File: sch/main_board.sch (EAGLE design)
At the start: 19 parts, among them IC1 MCP73831T-2ACI_OT, J1 MICRO_USB_B_HIROSE_ZX62-B-5PA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

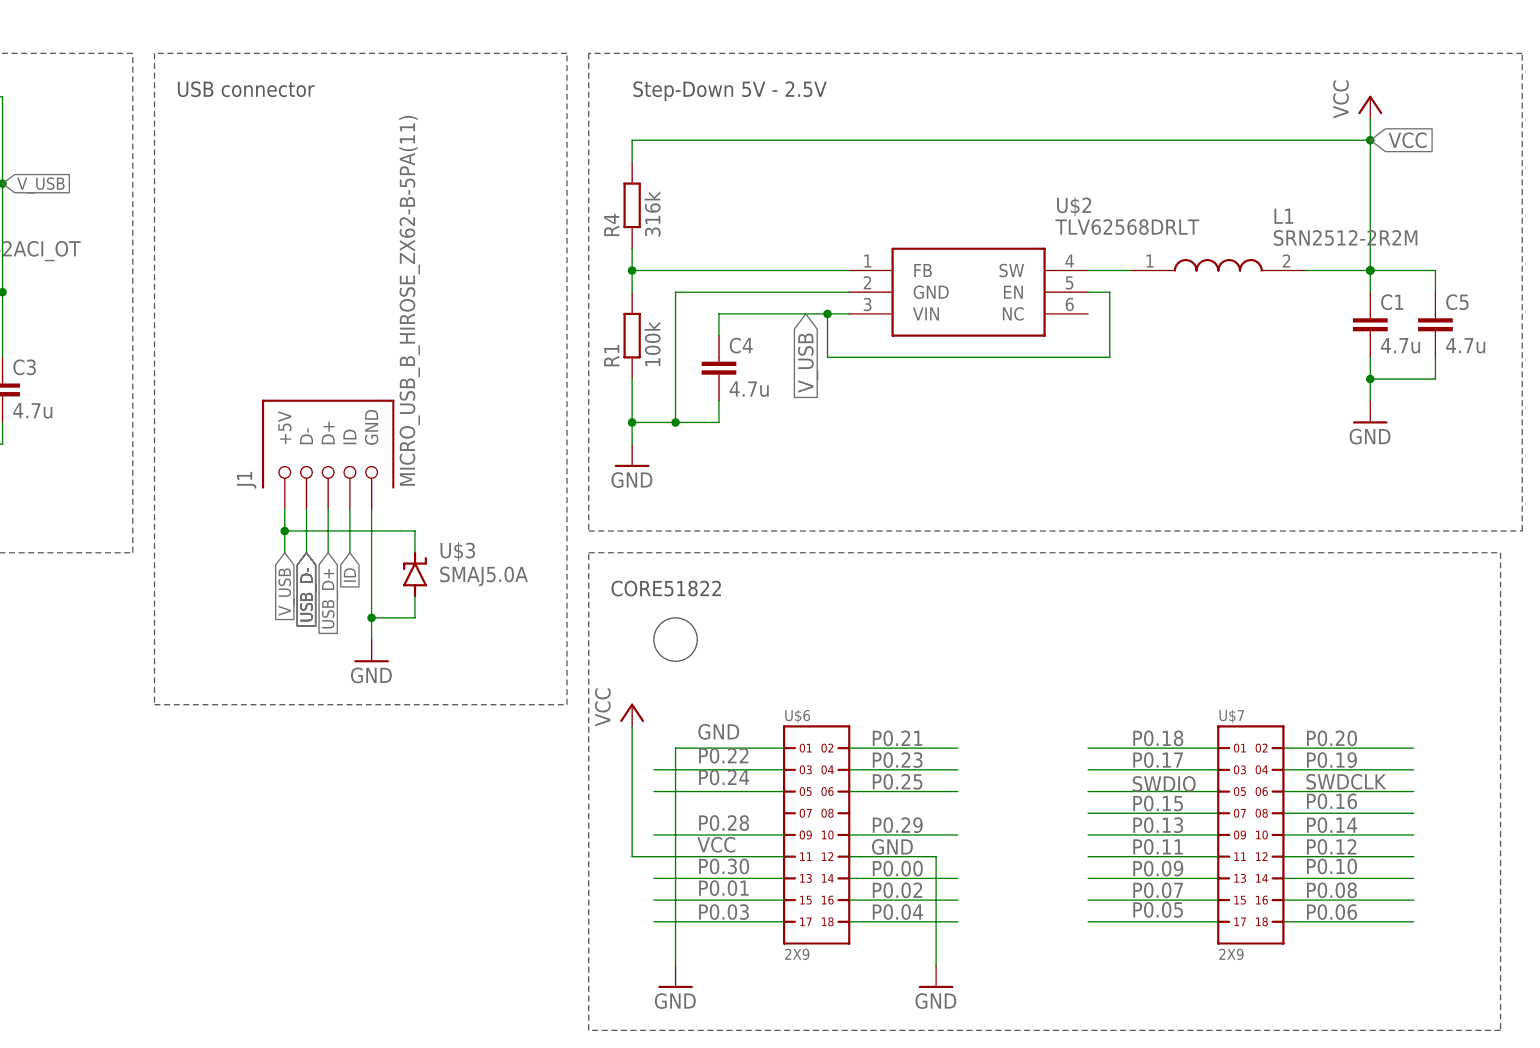
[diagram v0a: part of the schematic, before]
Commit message: Add docs for STM32WB, Remove unused power supply elements.
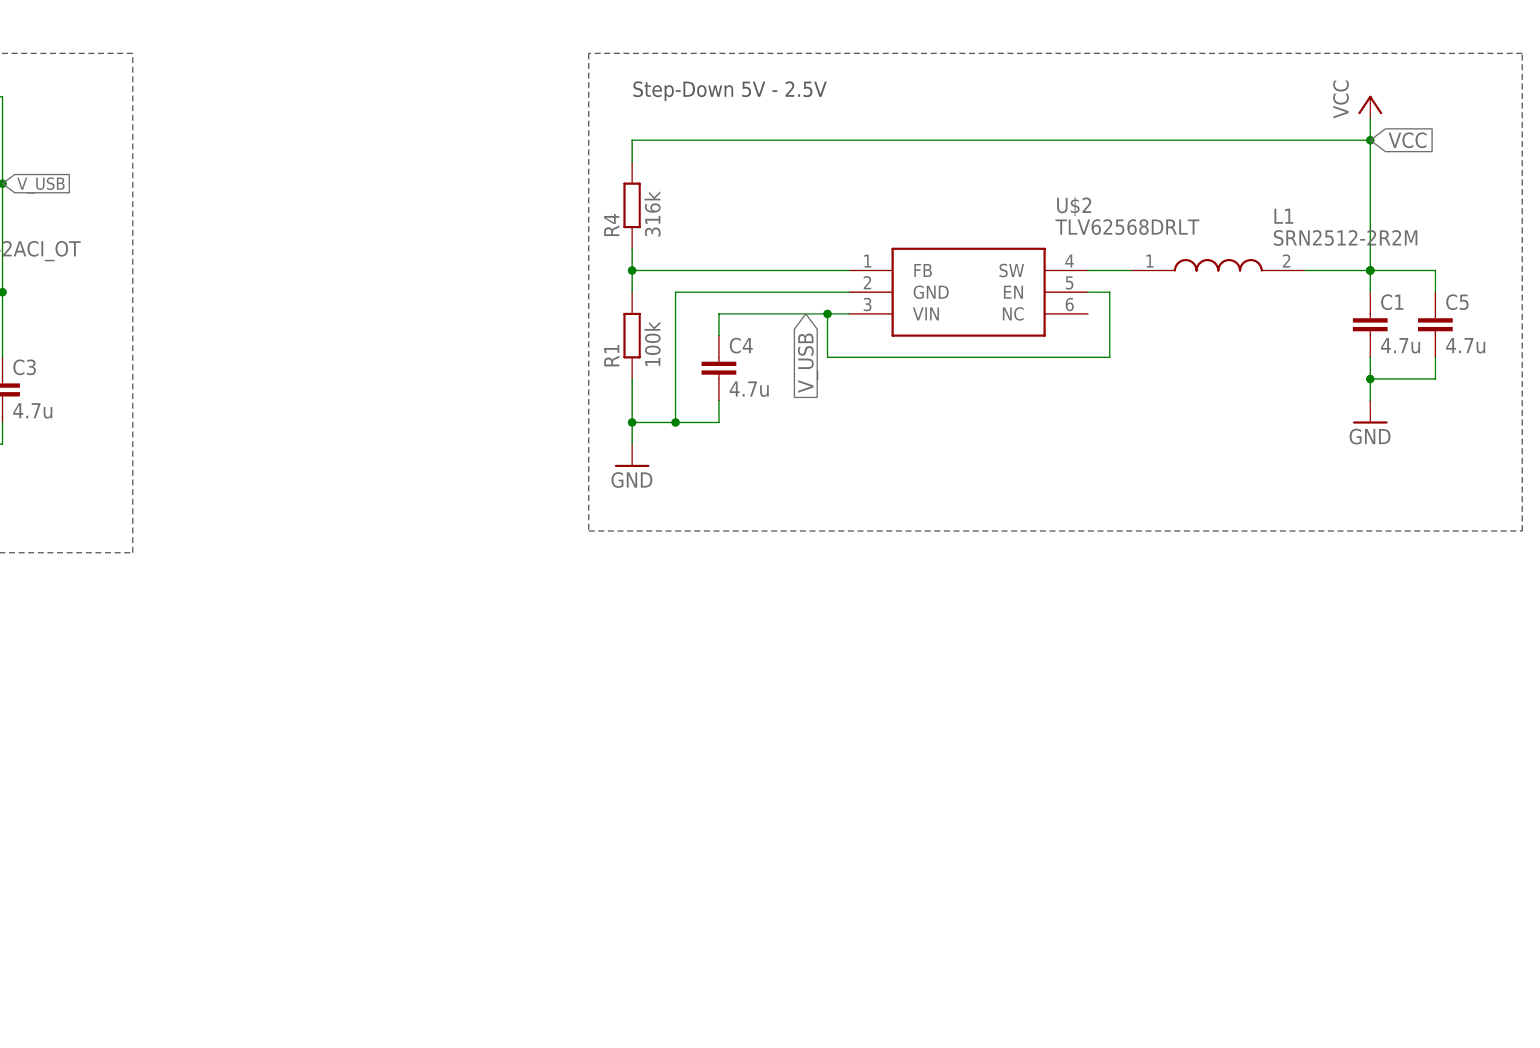
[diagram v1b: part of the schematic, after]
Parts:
- removed J1: MICRO_USB_B_HIROSE_ZX62-B-5PA(11), connector:MICRO_USB_B_HIROSE_ZX62-B-5PA(11)
- removed U$3: SMAJ5.0A, SamacSys_Parts:SMAJ5.0A
- removed U$6, U$7: 2X9, headers(2mm):2X9
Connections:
- removed net ID: J1.ID
- removed net P0.00: U$6.14
- removed net P0.01: U$6.15
- removed net P0.02: U$6.16
- removed net P0.03: U$6.17
- removed net P0.04: U$6.18
- removed net P0.05: U$7.17
- removed net P0.06: U$7.18
- removed net P0.07: U$7.15
- removed net P0.08: U$7.16
- removed net P0.09: U$7.13
- removed net P0.10: U$7.14
- removed net P0.11: U$7.11
- removed net P0.12: U$7.12
- removed net P0.13: U$7.9
- removed net P0.14: U$7.10
- removed net P0.15: U$7.7
- removed net P0.16: U$7.8
- removed net P0.17: U$7.3
- removed net P0.18: U$7.1
- removed net P0.19: U$7.4
- removed net P0.20: U$7.2
- removed net P0.21: U$6.2
- removed net P0.22: U$6.3
- removed net P0.23: U$6.4
- removed net P0.24: U$6.5
- removed net P0.25: U$6.6
- removed net P0.28: U$6.9
- removed net P0.29: U$6.10
- removed net P0.30: U$6.13
- removed net SWDCLK: U$7.6
- removed net SWDIO: U$7.5
- removed net USB_D+: J1.D+
- removed net USB_D-: J1.D-
- net GND: no longer J1.GND, U$3.A, U$6.1, U$6.12
- net VCC: no longer U$6.11
- net V_USB: no longer J1.+5V, U$3.C
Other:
- note removed: "CORE51822"
- note removed: "USB connector"

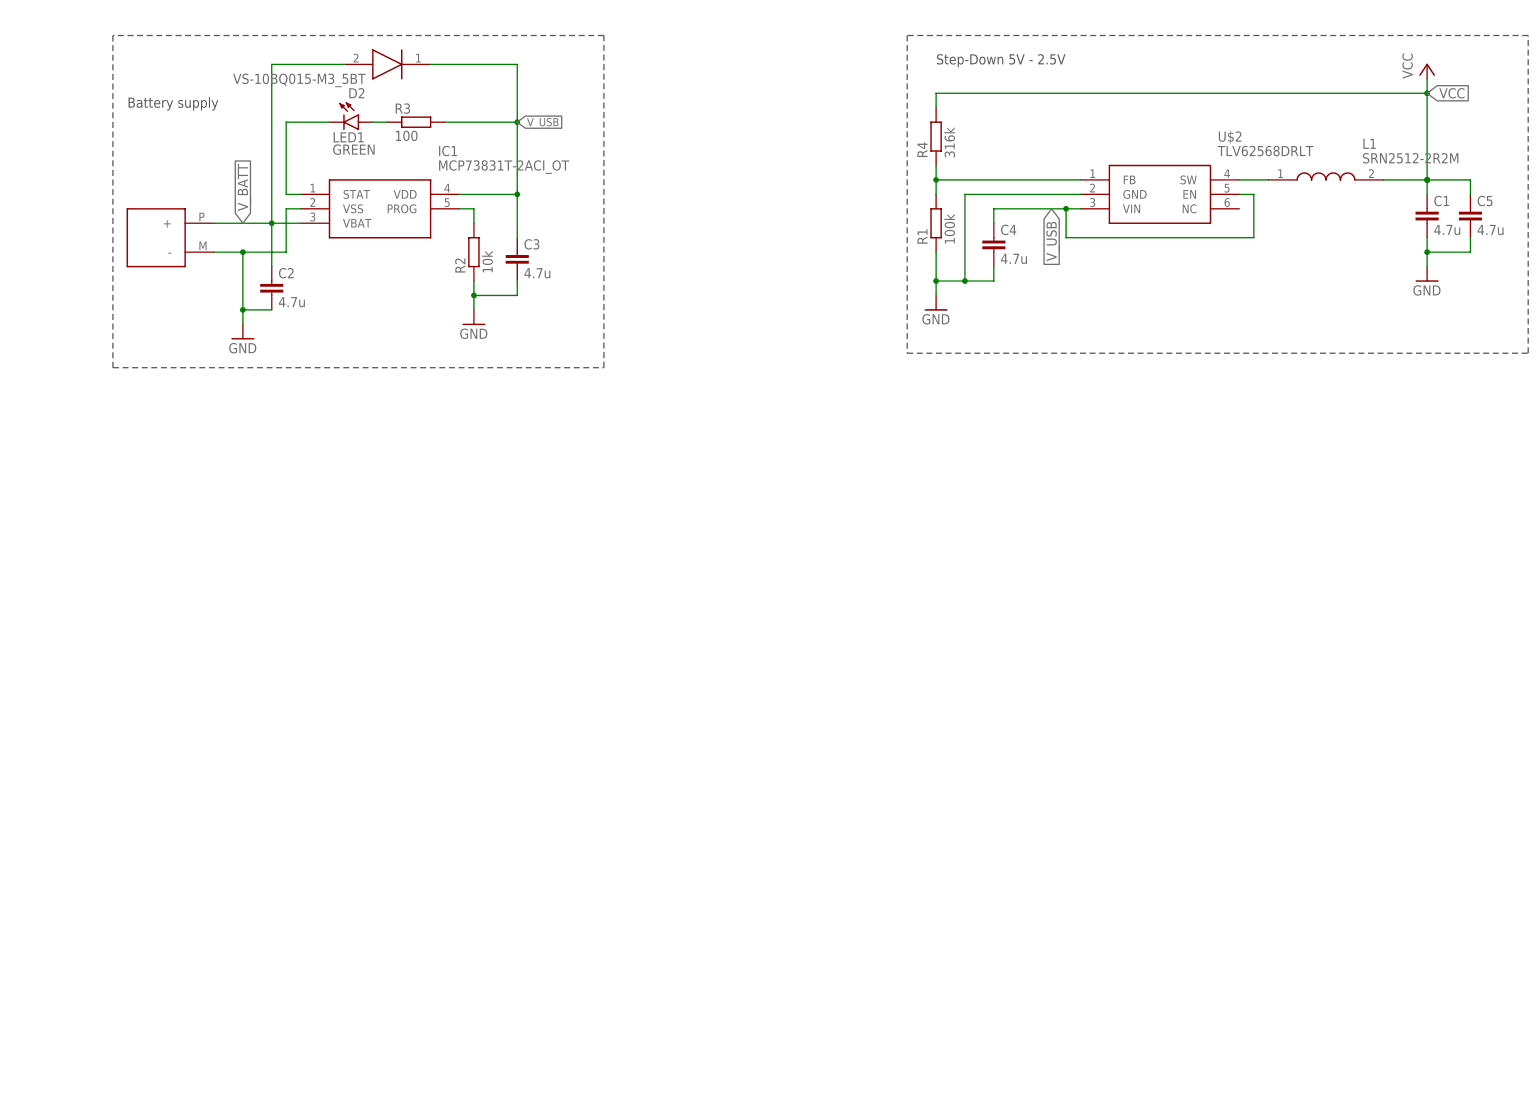
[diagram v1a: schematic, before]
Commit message: Add library for STM32WB prototype board.
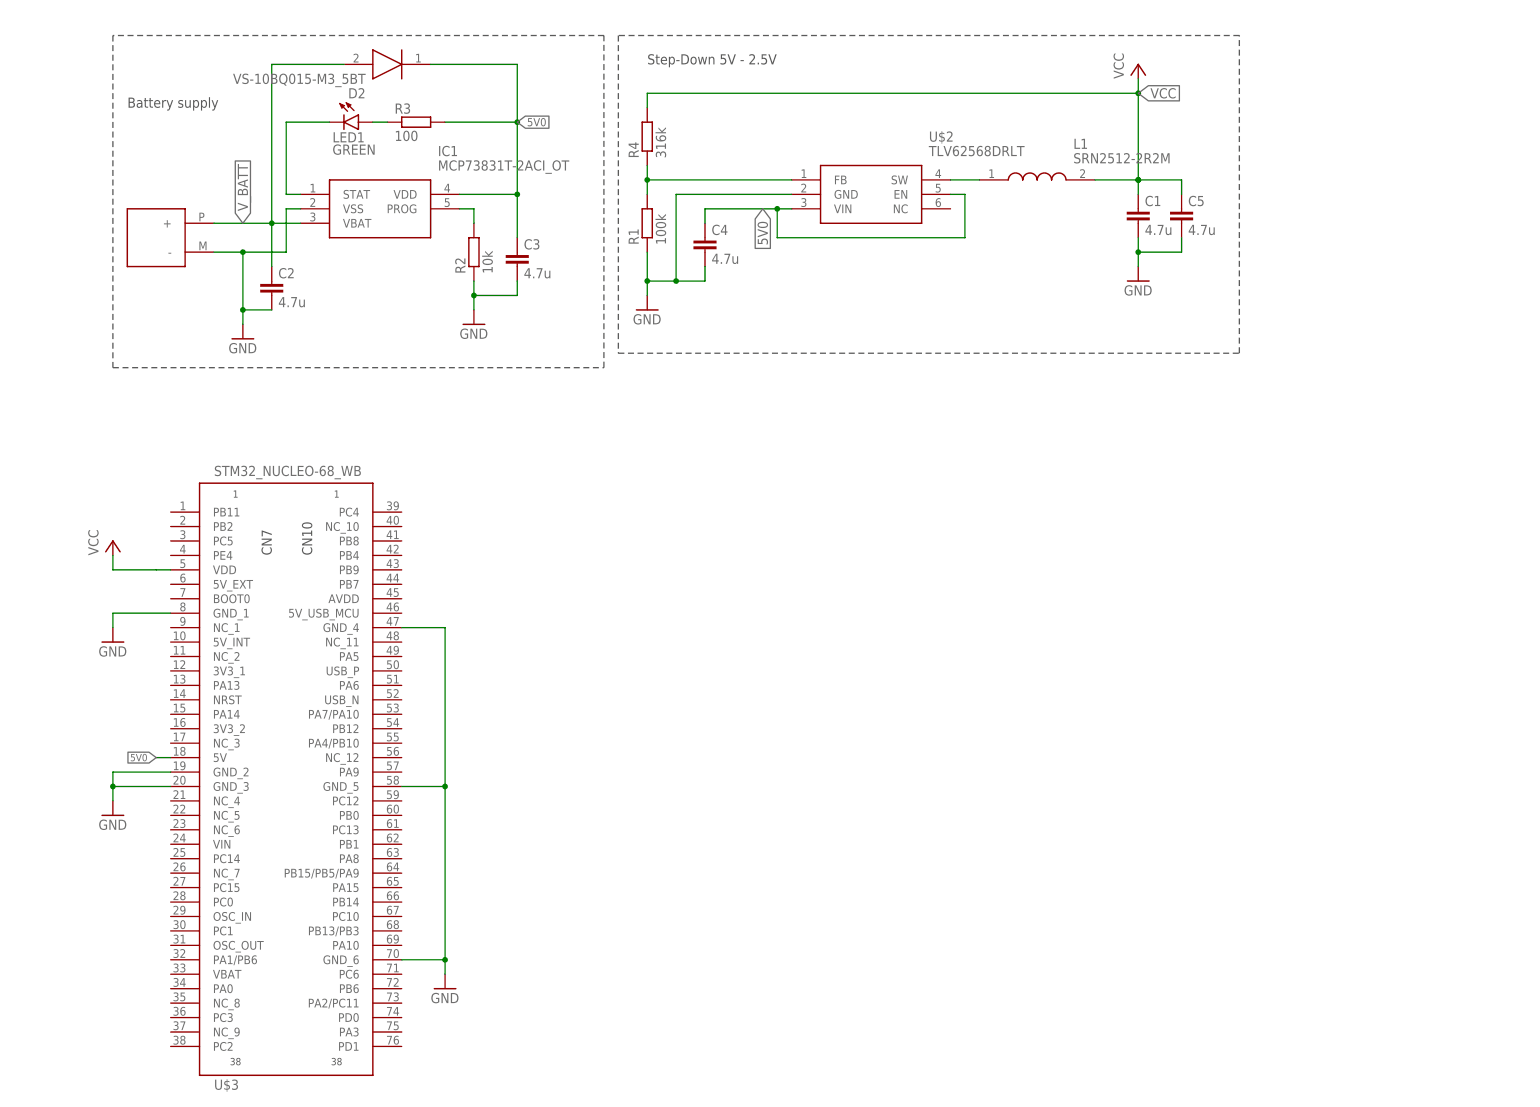
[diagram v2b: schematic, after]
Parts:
- added U$3: STM32_NUCLEO-68_WB, STM32WB:STM32_NUCLEO-68_WB
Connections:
- removed net V_USB: C3.1, C4.1, D2.K, IC1.VDD, R3.2, U$2.EN, U$2.VIN
- new net 5V0: C3.1, C4.1, D2.K, IC1.VDD, R3.2, U$2.EN, U$2.VIN, U$3.5V
- net GND: now also U$3.GND_1, U$3.GND_2, U$3.GND_3, U$3.GND_4, U$3.GND_5, U$3.GND_6
- net VCC: now also U$3.VDD
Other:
- moved on the sheet: C1, C4, C5, L1, R1, R4, U$2
